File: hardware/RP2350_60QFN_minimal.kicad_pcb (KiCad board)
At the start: 4 copper layers, 106.9 x 43.5 mm, 138 parts, among them J1 UJ20-C-H-G-SMT-2A-P16-TR, J2 73101-0570, J3 73101-0570, J4 PinHeader_1x03, J5 4677, SW1 SW_Push, SW2 SW_Push, U1 RP2350_60QFN, U10 ADG621BRMZ, U13 TLP3441TP_F, U15 ADG621BRMZ, U2 REF35330QDBVR, U3 W25Q128JVS, U4 LM27762, U5 NCP1117-3.3_SOT223, U6 MCP47FEB02A0T-E/ST, U7 Opamp_Dual, U8 TLP3441TP_F, Y1 ABM8-272-T3

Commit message: routed analog block
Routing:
- net /CHB_SELR2: track 0.00 -> 89.5 mm, vias 0 -> 2
- net /CHB_SELR1: track 0.00 -> 88.5 mm, vias 0 -> 2
- net /CHB_SELC: track 5.03 -> 77.6 mm, vias 0 -> 2
- net /CHA_ADC: track 0.00 -> 67.4 mm
- net /CHB_ADC: track 0.00 -> 54.3 mm, vias 0 -> 2
- net /CHA_SELC: track 0.00 -> 51.1 mm, vias 0 -> 2
- net -1V65: track 5.09 -> 55.5 mm, vias 5 -> 19
- net /VREF: track 41.9 -> 89.9 mm, vias 0 -> 3
- net /CHA_SELR1: track 0.00 -> 46.0 mm, vias 0 -> 2
- net /CHA_SELR2: track 0.00 -> 35.7 mm, vias 0 -> 2
- net +1V65: track 15.4 -> 44.2 mm, vias 7 -> 17
- net GND: track 55.8 -> 82.4 mm, vias 55 -> 76
- net Net-(U10-S1): track 0.00 -> 13.3 mm
- net Net-(U15-S1): track 0.00 -> 12.6 mm
- net +3V3A: track 3.98 -> 15.9 mm, vias 1 -> 9
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
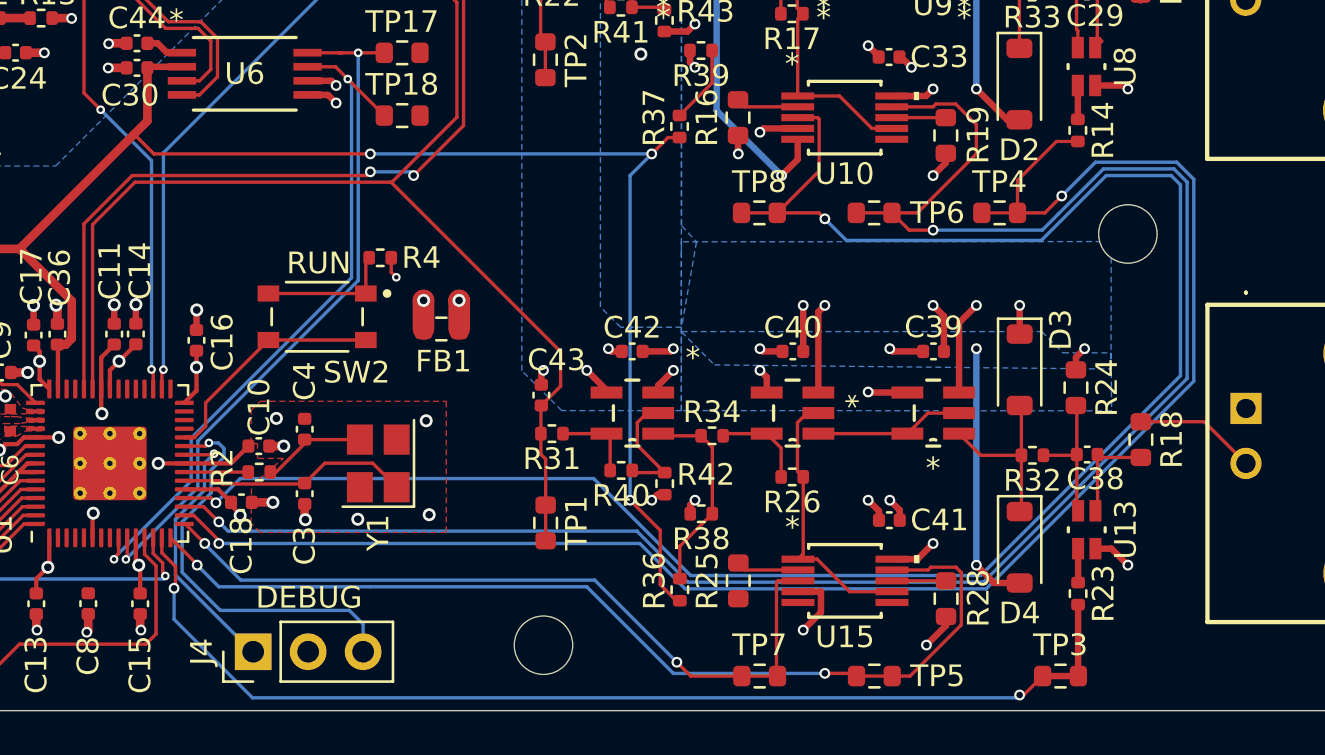
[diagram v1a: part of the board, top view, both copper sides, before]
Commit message: fixed vref routing and -1v65 for CHA switch
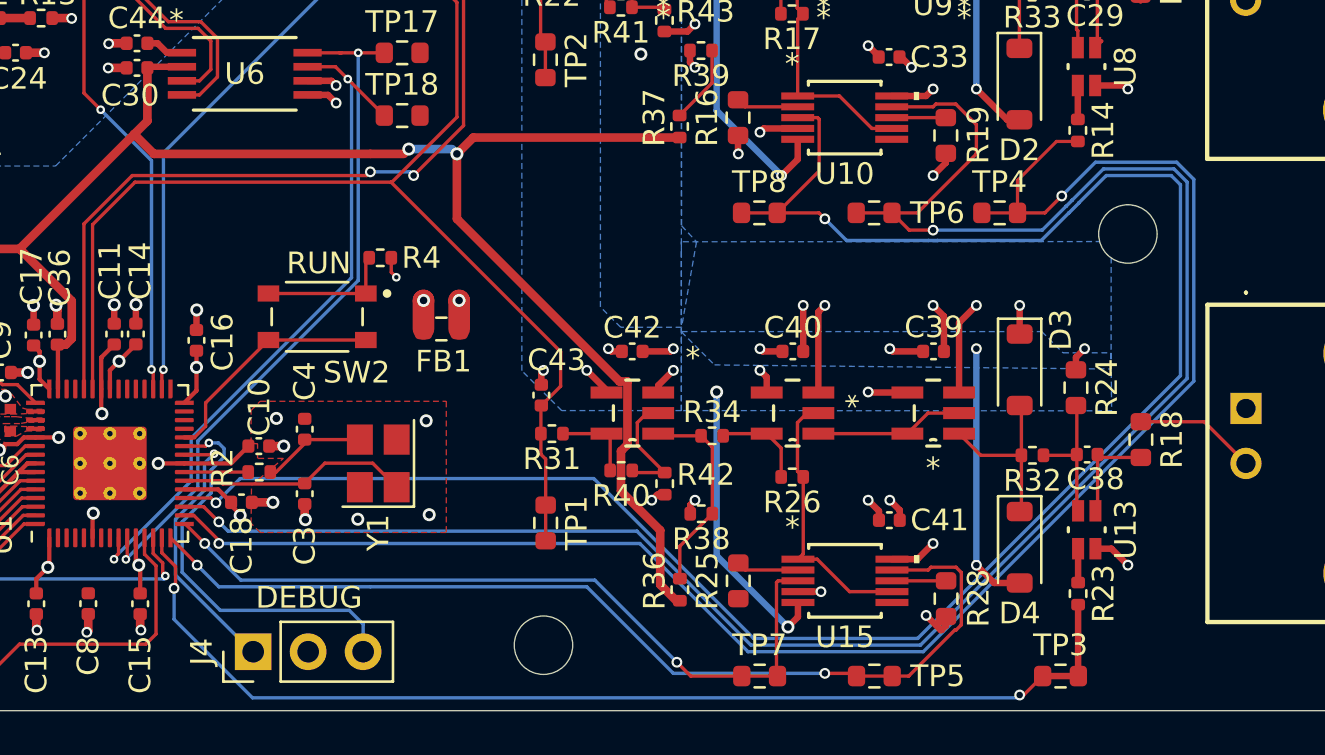
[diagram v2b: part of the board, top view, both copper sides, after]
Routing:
- net -1V65: track 55.5 -> 69.0 mm, vias 19 -> 21
- net /VREF: track 89.9 -> 93.5 mm, vias 3 -> 2
- net /CHB_SELR2: track 89.5 -> 91.9 mm
- net /CHB_SELR1: track 88.5 -> 90.9 mm
- net /CHB_SELC: track 77.6 -> 80.0 mm
- net GND: track 82.4 -> 80.3 mm

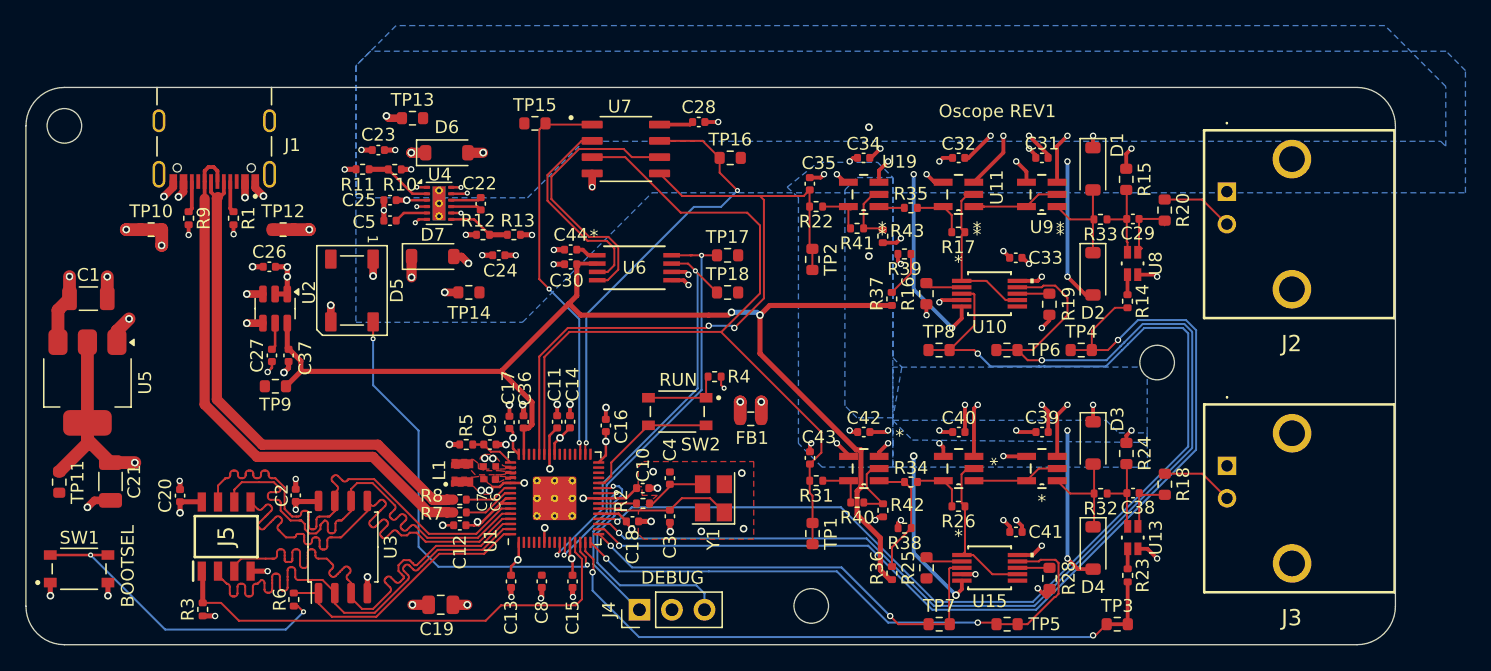
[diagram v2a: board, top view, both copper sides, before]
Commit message: feat(hardware): Fix unconnected nets
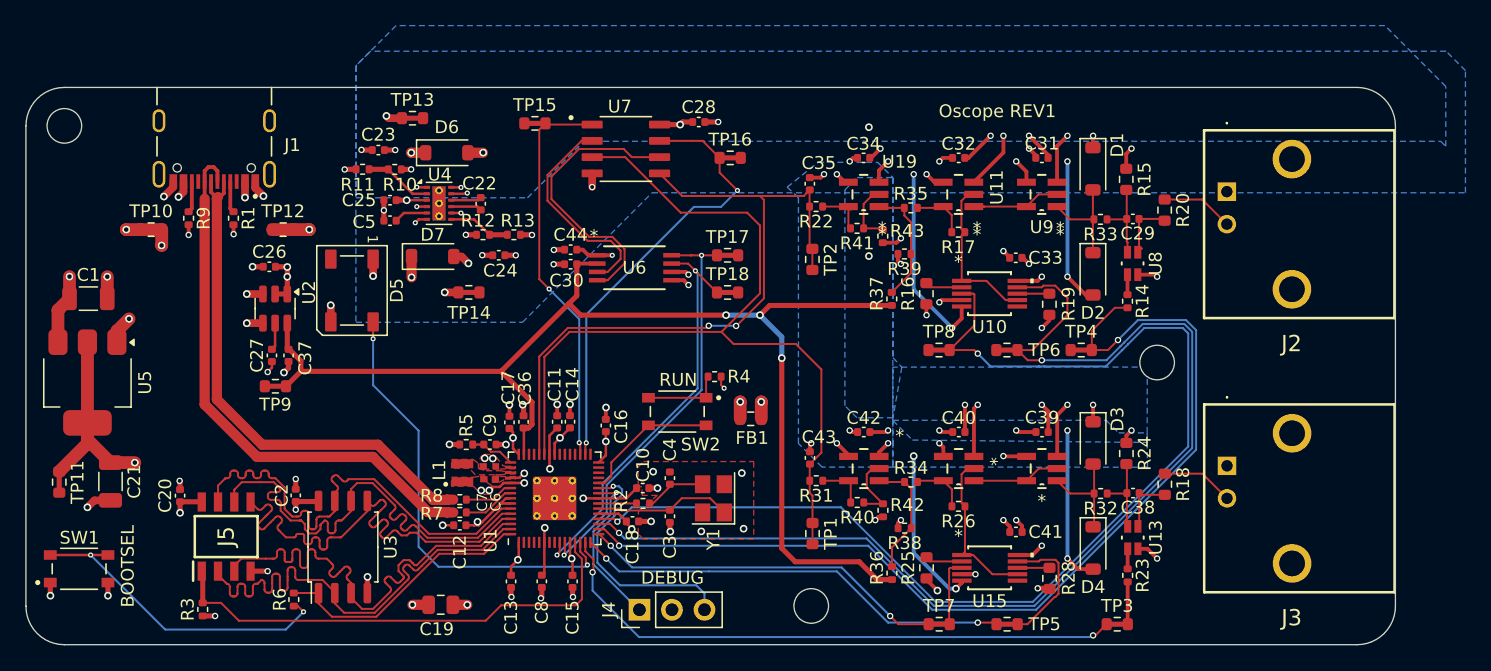
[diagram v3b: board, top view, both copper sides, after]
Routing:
- net +3V3: track 48.6 -> 53.6 mm, vias 14 -> 16
- net /VREF: track 93.5 -> 98.1 mm, vias 2 -> 3
- net /Analog Frontend Channel B/OFFSET_REF: track 5.64 -> 9.46 mm
- net /CHA_ADC: track 67.4 -> 70.2 mm
- net +1V1: track 15.8 -> 18.4 mm
- net /CHB_TRIG: track 35.1 -> 36.8 mm
- net /CHA_TRIG: track 31.0 -> 32.7 mm
- net +1V65: track 44.2 -> 45.8 mm
- net /TRIG_SDA: track 32.4 -> 34.0 mm
- net /TRIG_SCL: track 32.5 -> 34.2 mm
- net -1V65: track 69.0 -> 70.0 mm
- net /Trigger/CHA_COMP: track 16.2 -> 16.8 mm
- net /Trigger/CHB_COMP: track 21.9 -> 22.5 mm
- net GND: track 80.3 -> 80.9 mm, vias 76 -> 77
- net +3V3A: vias 9 -> 10
